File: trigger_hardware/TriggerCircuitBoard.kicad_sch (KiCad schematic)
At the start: 29 parts, among them J1 Screw_Terminal_01x02, J10 Conn_02x15_Odd_Even, J11 Conn_02x15_Odd_Even, J12 Conn_Coaxial, J13 Conn_Coaxial, J14 Conn_Coaxial, J2 Conn_02x05_Odd_Even, J3 Conn_Coaxial, J4 Screw_Terminal_01x04, J5 Screw_Terminal_01x04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

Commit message: update circuit design
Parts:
- added C2: C, symbol Device:C
- A1: value Arduino_Nano_ESP32 -> Arduino Nano ESP32
- D1: value LED_BRKG -> Status LED
- DISP1: renamed from OLED_Display1; value ~ -> Status Display
- J1: renamed from J10; value Conn_02x15_Odd_Even -> Arduino Header Pins 1
- J11: renamed from J3; value Conn_Coaxial -> Coaxial Plug
- J12, J13, J14: value Conn_Coaxial -> Coaxial Plug
- J2: renamed from J11; value Conn_02x15_Odd_Even -> Arduino Header Pins 2
- J20: renamed from J9; value Screw_Terminal_01x04 -> Screw Terminal
- J3: renamed from J2; value Conn_02x05_Odd_Even -> CCS Controller IO
- J4: renamed from J1; value Screw_Terminal_01x02 -> 24VDC Input Screw Terminal
- J5: renamed from J4; value Screw_Terminal_01x04 -> Screw Terminal
- J6: renamed from J5; value Screw_Terminal_01x04 -> Screw Terminal
- J7: renamed from J6; value Screw_Terminal_01x04 -> Screw Terminal
- J8: renamed from J7; value Screw_Terminal_01x04 -> Screw Terminal
- J9: renamed from J8; value Screw_Terminal_01x04 -> Screw Terminal
- SW1: value SW_DPST -> On/Off Switch
- SW2: value SW_Push -> Reset Button
- renumbered R4 to R1, R5 to R2, R6 to R3, R1 to R4, R2 to R5, R3 to R6
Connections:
- net 3V3: now also C2.1
- net GND: now also C2.2
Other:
- moved on the sheet: A1, C1, J4, SW1, SW2

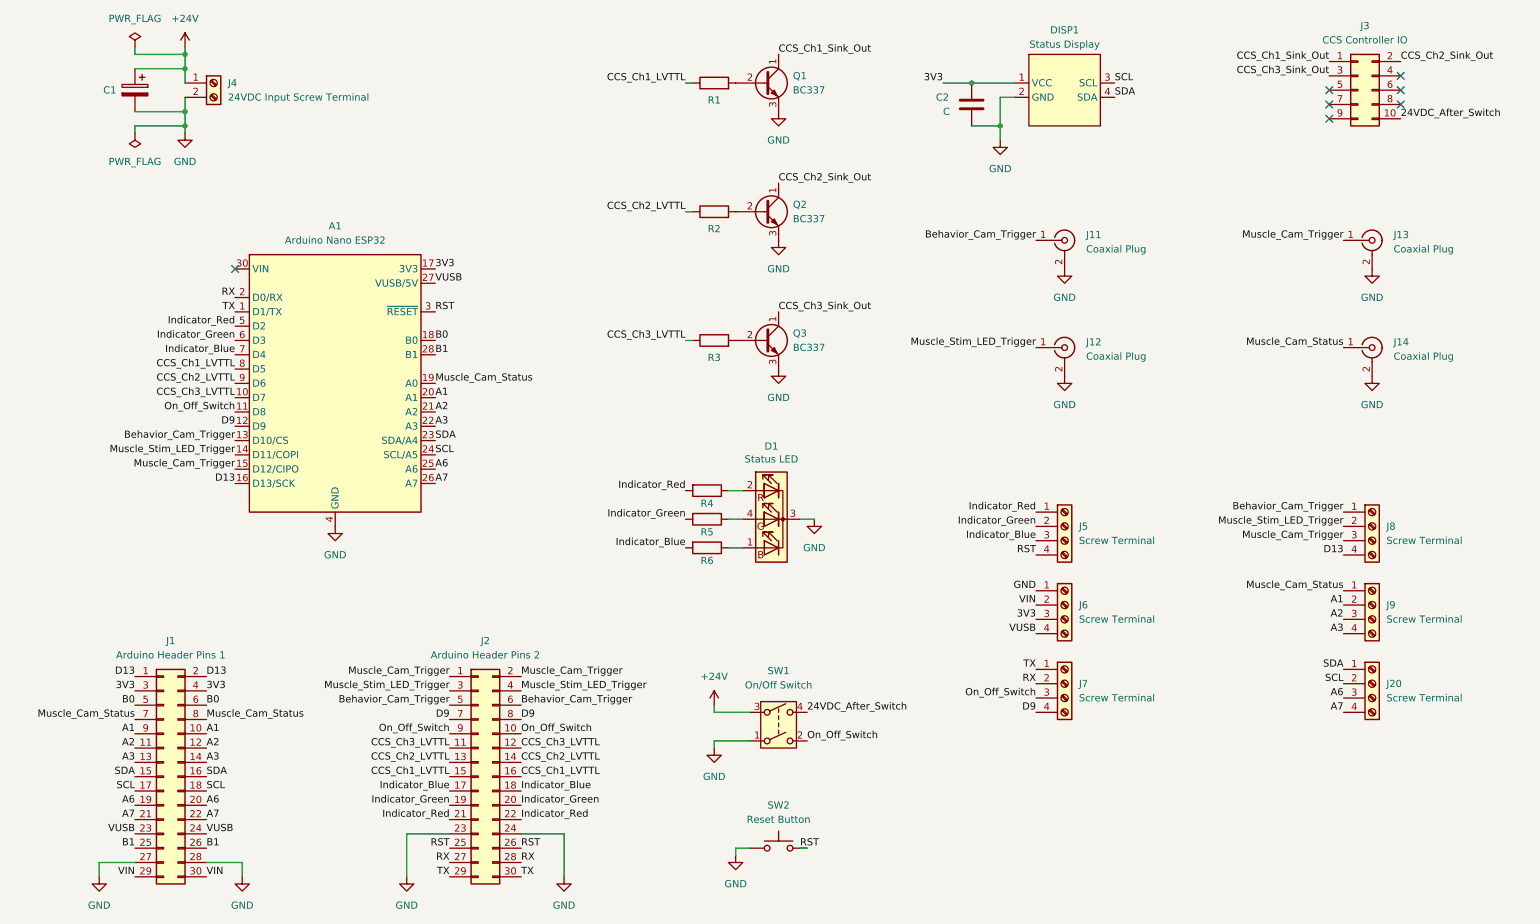
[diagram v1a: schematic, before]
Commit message: update trigger hardware
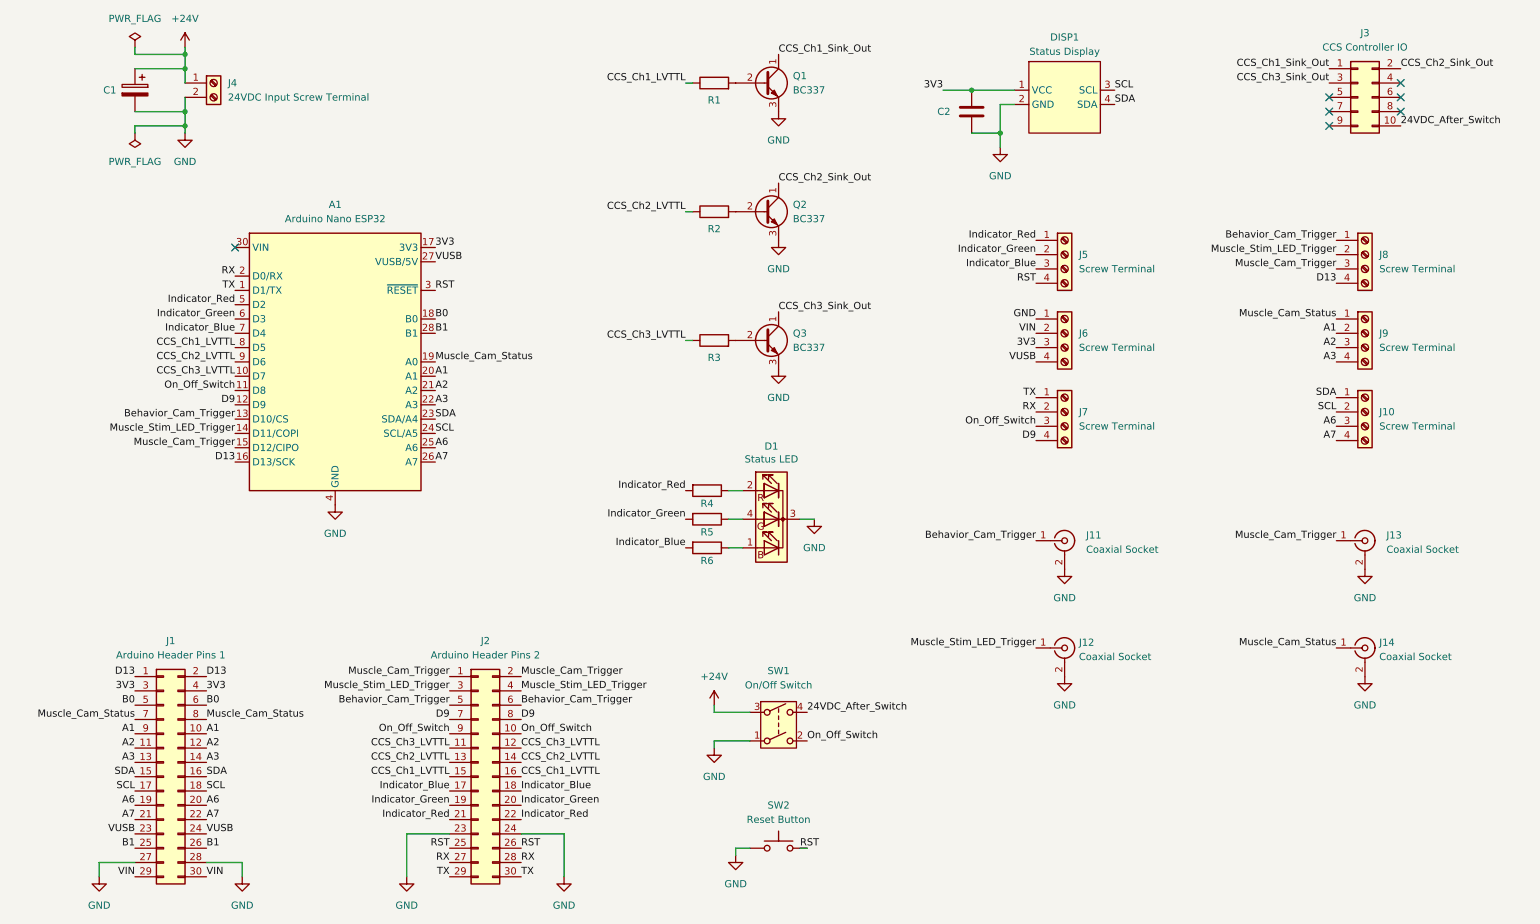
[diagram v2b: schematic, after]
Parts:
- J11, J12, J13, J14: value Coaxial Plug -> Coaxial Socket
- renumbered J20 to J10
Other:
- moved on the sheet: A1, C2, DISP1, J10, J11, J12, J13, J14, J3, J5, J6, J7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

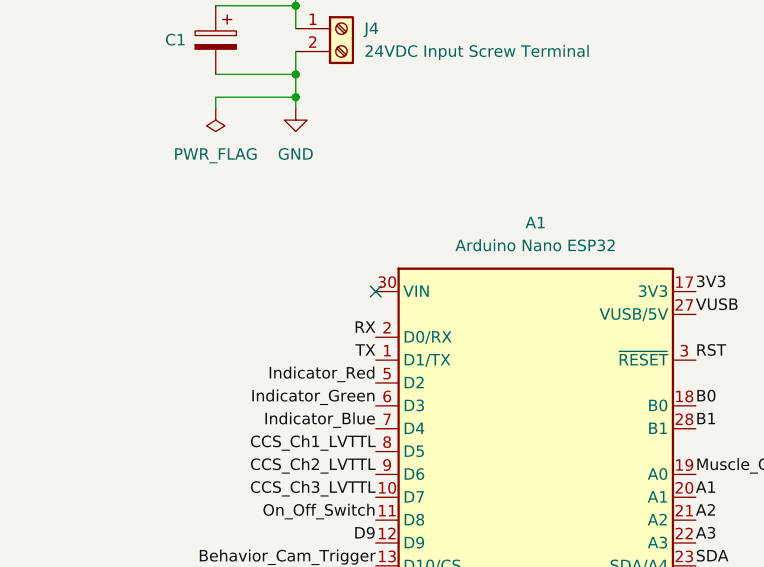
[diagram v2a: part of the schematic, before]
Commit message: update trigger circuit schematics
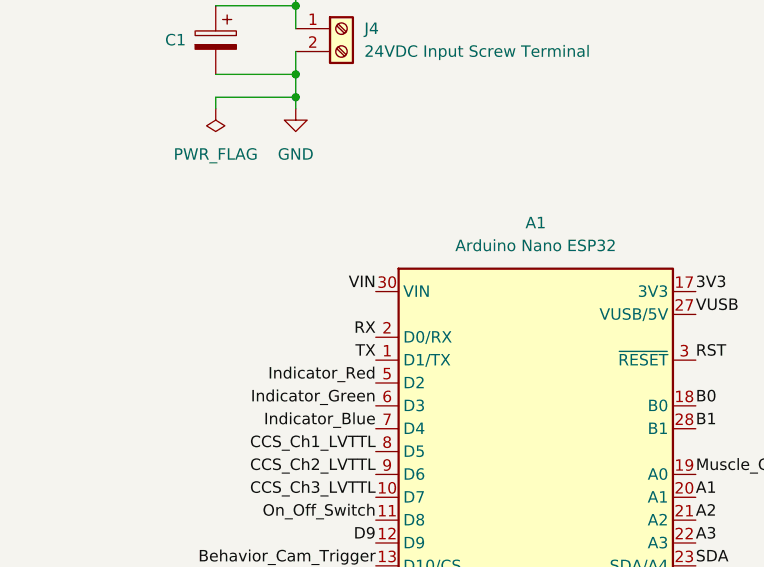
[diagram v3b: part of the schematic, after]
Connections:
- net VIN: now also A1.30 (VIN)
- no-connect marks 7 -> 6
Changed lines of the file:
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@@
-	)
-	(no_connect
-		(at 52.07 64.77)
 	)
 	(no_connect
@@
 		(effects
 			(font
+				(size 1.27 1.27)
+			)
+			(justify right bottom)
+		)
+	)
+	(label "VIN"
+		(at 52.07 64.77 180)
+		(effects
+			(font
